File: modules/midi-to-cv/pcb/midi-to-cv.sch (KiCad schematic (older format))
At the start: 47 parts, among them J1 MIDI in, J2 DEBUG HEADER, J3 CV1, J4 CV2, J5 CV3, J6 CV4, J7 GATE1, J8 GATE2, J9 Conn_02x08_Odd_Even, U1 6N137, U2 ATtiny4313-PU, U3 MCP4822, U4 MCP4822, U5 LM324, Y1 20mhz

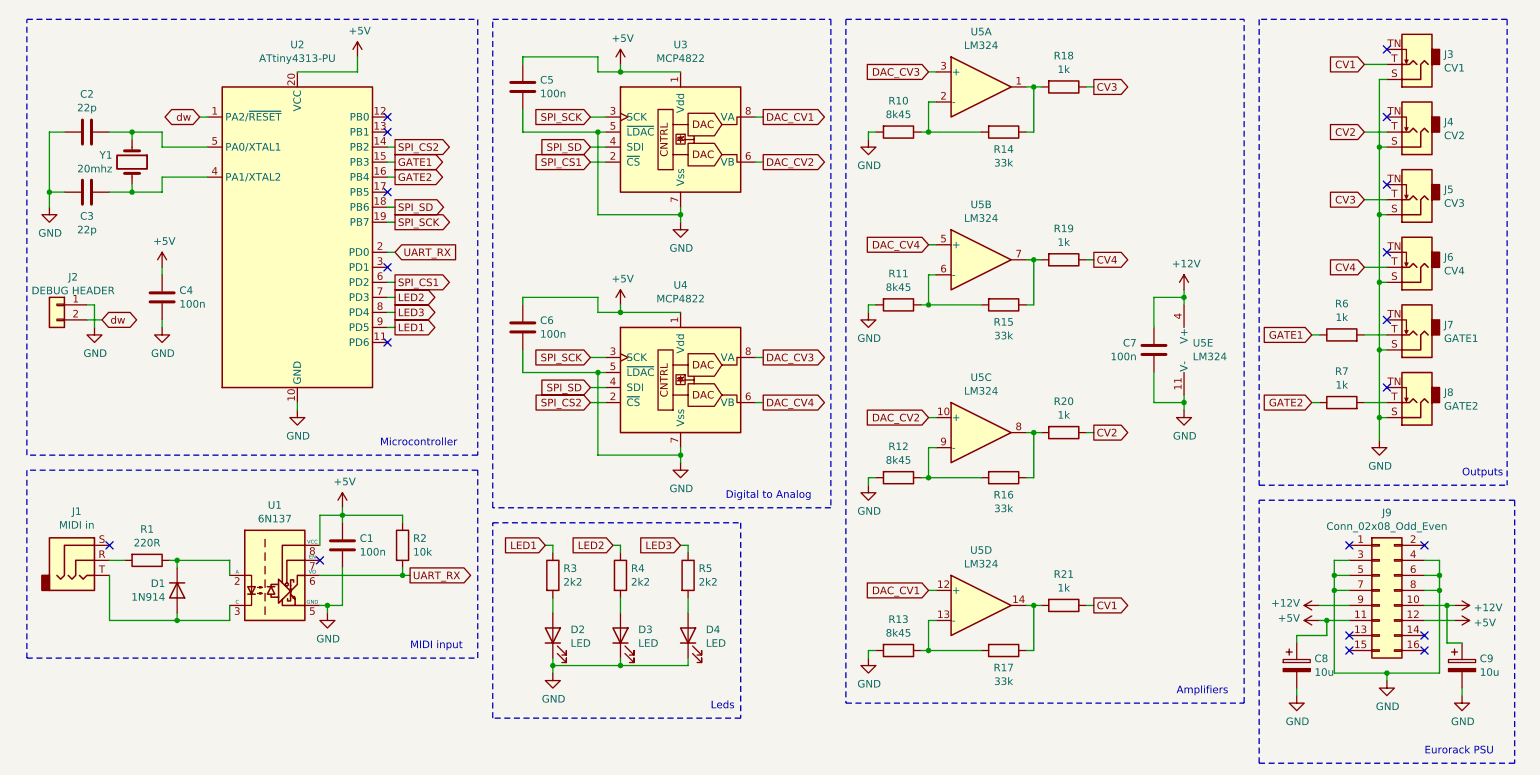
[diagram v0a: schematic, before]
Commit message: modules: midi-to-cv: fix references
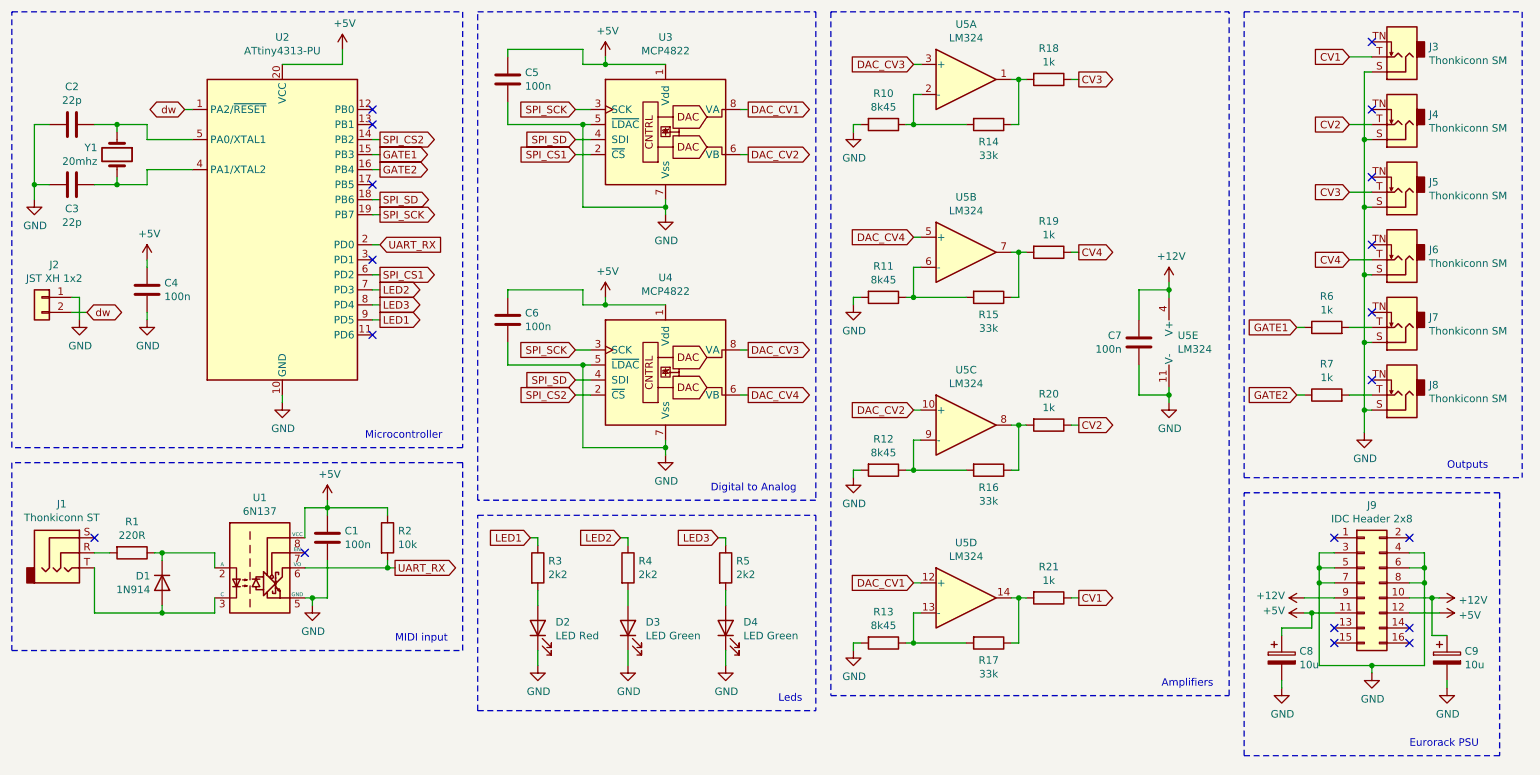
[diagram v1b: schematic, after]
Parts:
- D2: value LED -> LED Red
- D3, D4: value LED -> LED Green
- J1: value MIDI in -> Thonkiconn ST
- J2: value DEBUG HEADER -> JST XH 1x2
- J3: value CV1 -> Thonkiconn SM
- J4: value CV2 -> Thonkiconn SM
- J5: value CV3 -> Thonkiconn SM
- J6: value CV4 -> Thonkiconn SM
- J7: value GATE1 -> Thonkiconn SM
- J8: value GATE2 -> Thonkiconn SM
- J9: value Conn_02x08_Odd_Even -> IDC Header 2x8
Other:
- moved on the sheet: C1, C2, C3, C4, C5, C6, C7, C8, C9, D1, D2, D3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
